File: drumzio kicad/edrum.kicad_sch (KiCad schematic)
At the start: 14 parts, among them J1 Piezo connector

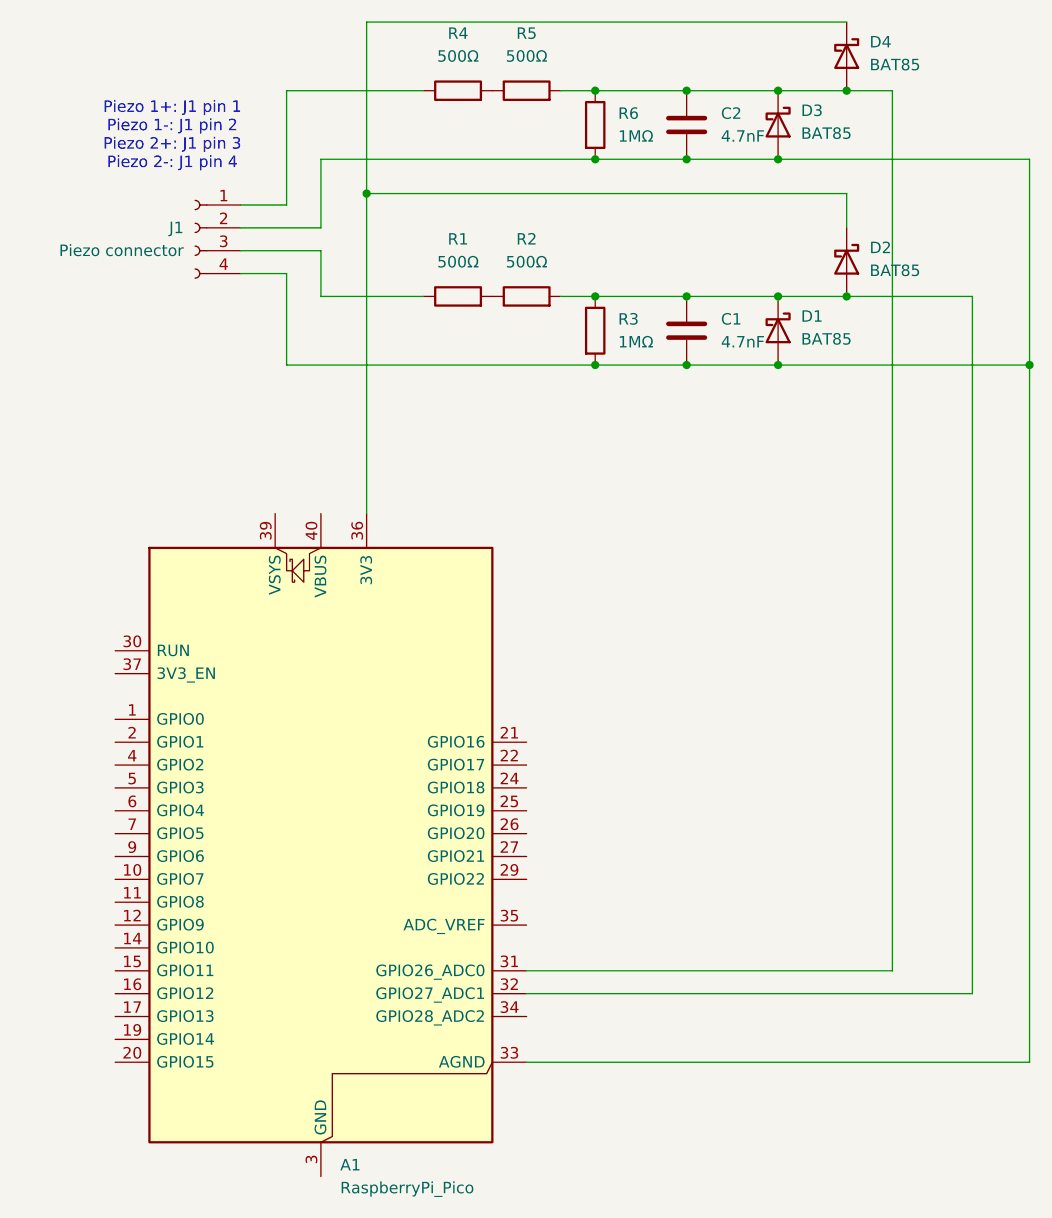
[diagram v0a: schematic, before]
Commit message: new electronics for better hit detection
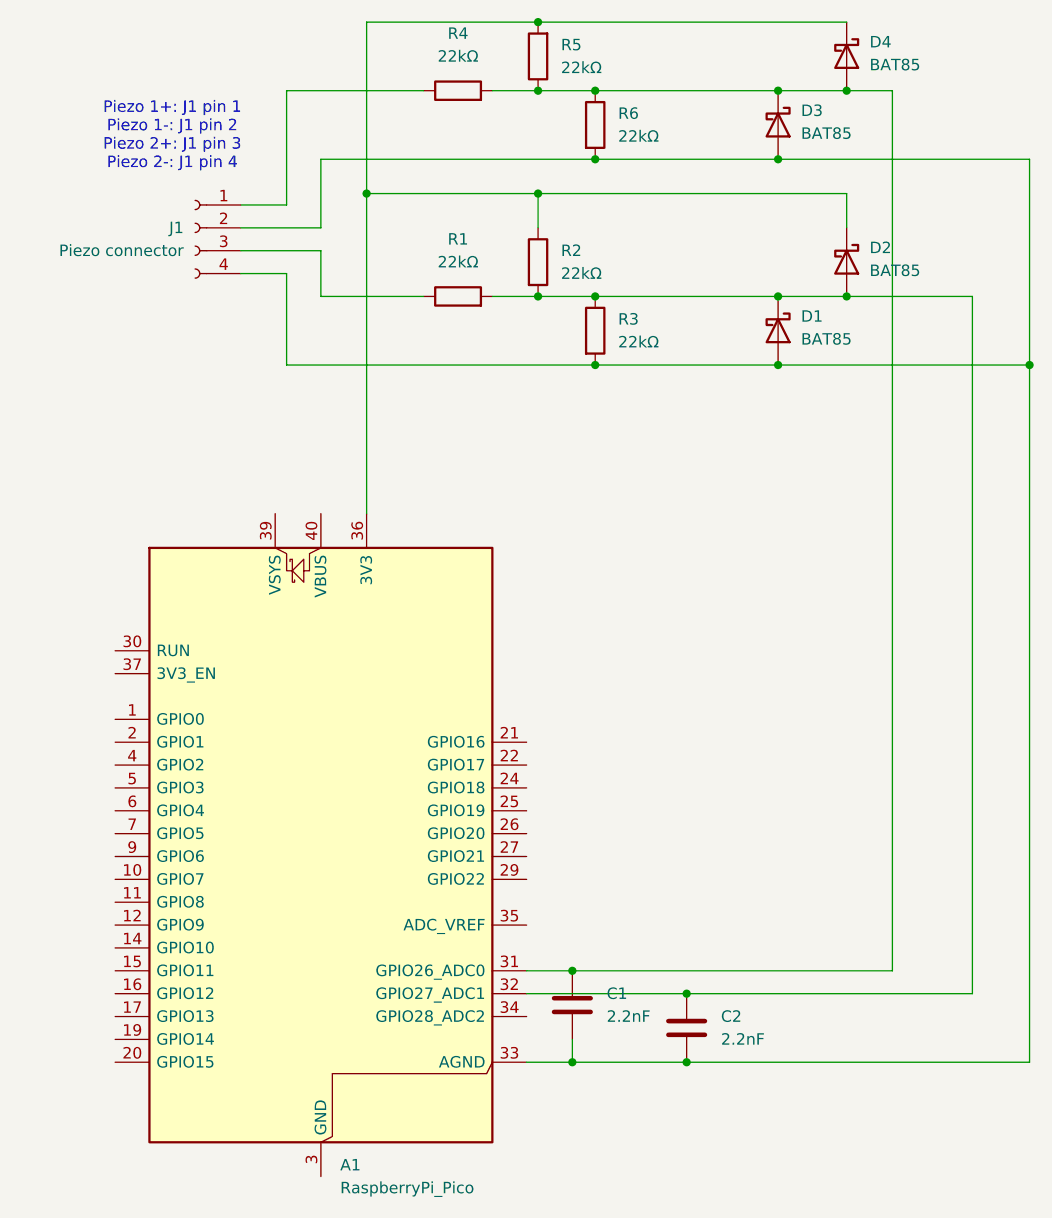
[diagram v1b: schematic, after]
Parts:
- C1, C2: value 4.7nF -> 2.2nF
- R1, R2, R4, R5: value 500Ω -> 22kΩ
- R3, R6: value 1MΩ -> 22kΩ
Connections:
- net at R1.2: now also A1.32 (GPIO27_ADC1), C2.1, D1.1 (K), D2.2 (A), R2.2, R3.1; no longer R2.1
- net at A1.31 (GPIO26_ADC0), D3.1 (K), D4.2 (A)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: now also C1.1, R4.2, R5.1; no longer C2.1, R5.2
- net at A1.36 (3V3), D2.1 (K), D4.1 (K): now also R2.1, R5.2
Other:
- moved on the sheet: C1, C2, R2, R5
